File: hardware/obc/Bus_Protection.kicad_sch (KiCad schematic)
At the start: 42 parts, among them Q201 BSS138DWQ-7, Q202 BSS138DWQ-7, Q203 MBT2222ADW1T1, Q204 MBT2222ADW1T1, Q205 BSS138DWQ-7, Q206 BSS138DWQ-7, Q207 MBT2222ADW1T1, Q208 MBT2222ADW1T1, Q209 MMDT2907

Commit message: obc: adjust part numbers for resistors
Many of selected variants are difficult to source for assembly.
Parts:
- R203, R204, R213, R214: LCSC C4244464 -> C112310; Manufacturer_Name Vishay Intertech -> (none); Manufacturer_Part_Number CRCW0603680RJNEA -> (none)
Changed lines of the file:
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@@
 			)
 		)
-		(property "LCSC" "C4244464"
+		(property "LCSC" "C112310"
 			(at 39.37 66.04 0)
 			(effects
@@
 			)
 		)
-		(property "Manufacturer_Name" " Vishay Intertech"
+		(property "Manufacturer_Name" ""
 			(at 39.37 66.04 0)
 			(effects
@@
 			)
 		)
-		(property "Manufacturer_Part_Number" " CRCW0603680RJNEA"
+		(property "Manufacturer_Part_Number" ""
 			(at 39.37 66.04 0)
 			(effects
@@
 			)
 		)
-		(property "LCSC" "C4244464"
+		(property "LCSC" "C112310"
 			(at 81.28 66.04 0)
 			(effects
@@
 			)
 		)
-		(property "Manufacturer_Name" " Vishay Intertech"
+		(property "Manufacturer_Name" ""
 			(at 81.28 66.04 0)
 			(effects
@@
 			)
 		)
-		(property "Manufacturer_Part_Number" " CRCW0603680RJNEA"
+		(property "Manufacturer_Part_Number" ""
 			(at 81.28 66.04 0)
 			(effects
@@
 			)
 		)
-		(property "LCSC" "C4244464"
+		(property "LCSC" "C112310"
 			(at 39.37 144.78 0)
 			(effects
@@
 			)
 		)
-		(property "Manufacturer_Name" " Vishay Intertech"
+		(property "Manufacturer_Name" ""
 			(at 39.37 144.78 0)
 			(effects
@@
 			)
 		)
-		(property "Manufacturer_Part_Number" " CRCW0603680RJNEA"
+		(property "Manufacturer_Part_Number" ""
 			(at 39.37 144.78 0)
 			(effects
@@
 			)
 		)
-		(property "LCSC" "C4244464"
+		(property "LCSC" "C112310"
 			(at 81.28 144.78 0)
 			(effects
@@
 			)
 		)
-		(property "Manufacturer_Name" " Vishay Intertech"
+		(property "Manufacturer_Name" ""
 			(at 81.28 144.78 0)
 			(effects
@@
 			)
 		)
-		(property "Manufacturer_Part_Number" " CRCW0603680RJNEA"
+		(property "Manufacturer_Part_Number" ""
 			(at 81.28 144.78 0)
 			(effects

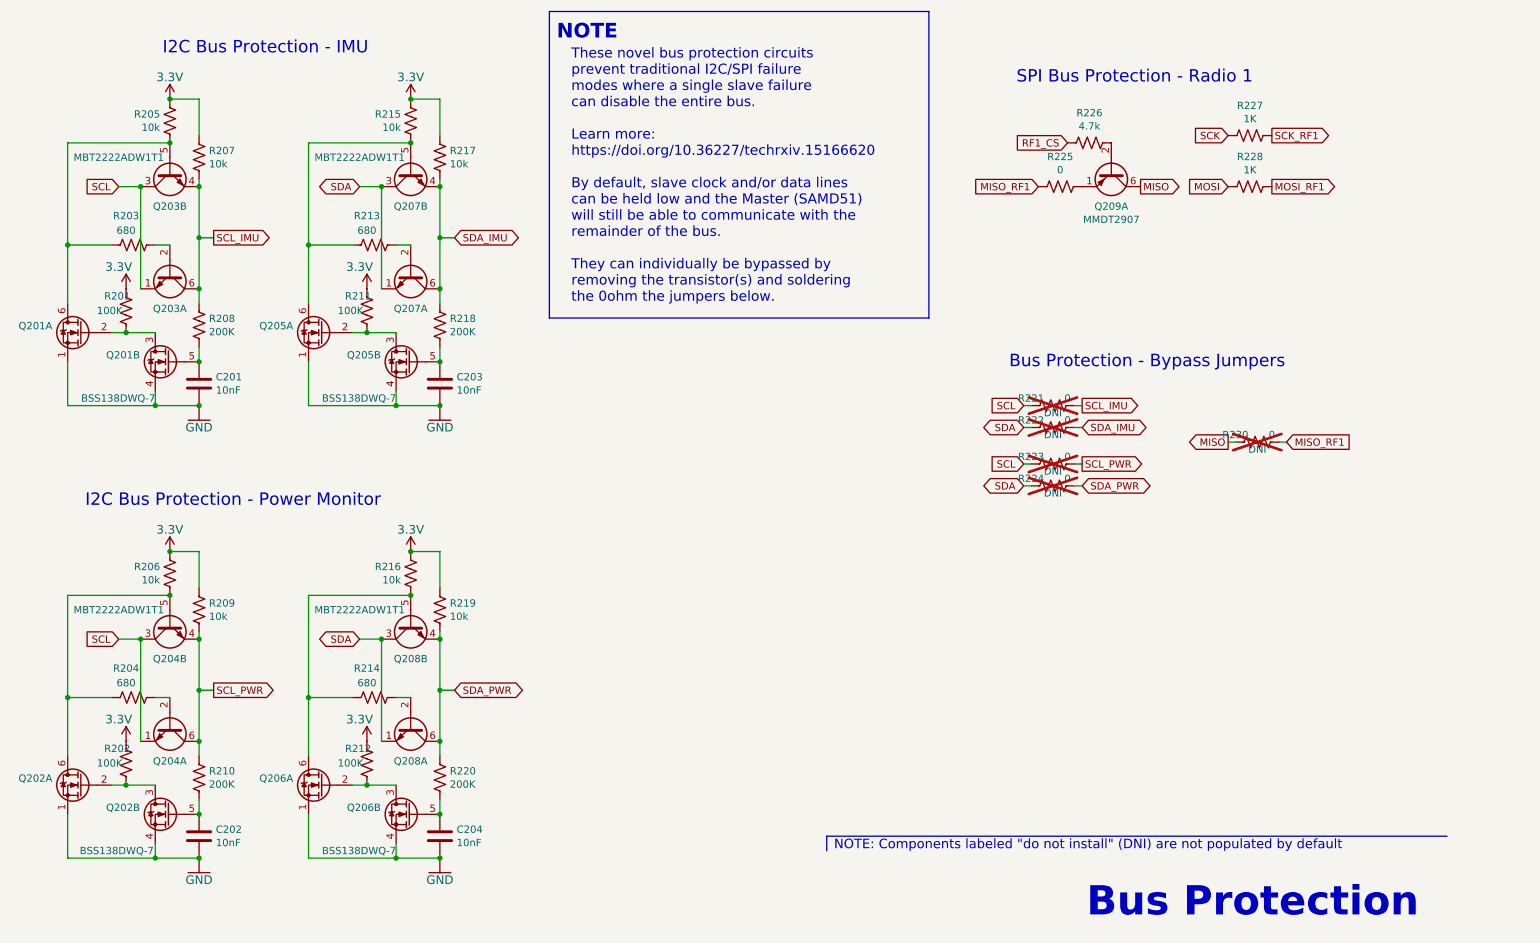
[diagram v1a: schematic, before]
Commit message: obc: substitute transistors based on study of datasheets
We have struggled with availability and made these substitutions.
Same footprint, so layout doesn't change:

ON BSS138DWQ-7-F -> Nexperia BSS138PS,115

ON MMDT2907AQ-7-F -> Nexperia BC857BS,115
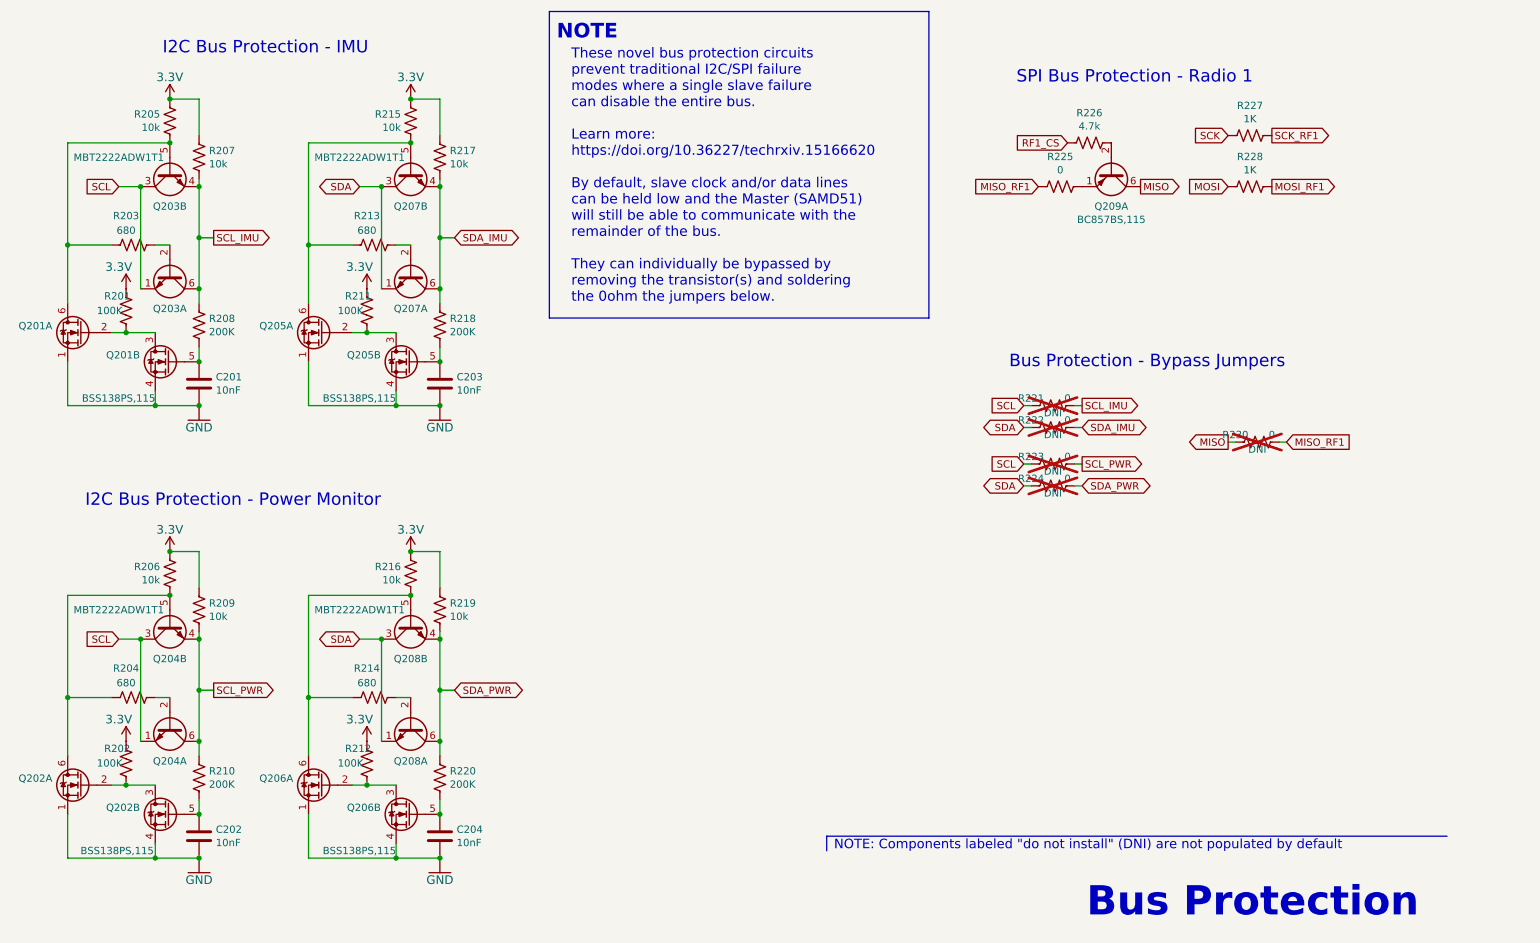
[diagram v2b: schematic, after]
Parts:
- Q201, Q202, Q205, Q206: value BSS138DWQ-7 -> BSS138PS,115; Flight BSS138DWQ-7 -> BSS138PS,115; LCSC C3280240 -> C193381; Manufacturer_Name Diodes Incorporated -> (none); Manufacturer_Part_Number BSS138DWQ-7 -> BSS138PS,115; Proto BSS138DWQ-7 -> BSS138PS,115
- Q209: value MMDT2907 -> BC857BS,115; Flight MMDT2907AQ-7-F -> BC857BS,115; LCSC C526684 -> C8654; Manufacturer_Name Diodes Incorporated -> (none); Manufacturer_Part_Number MMDT2907AQ-7-F -> BC857BS,115; Proto MMDT2907A -> BC857BS,115
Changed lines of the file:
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@@
 			)
 		)
-		(property "Value" "BSS138DWQ-7"
+		(property "Value" "BSS138PS,115"
 			(at 43.18 92.71 0)
 			(effects
@@
 			)
 		)
-		(property "Flight" "BSS138DWQ-7"
+		(property "Flight" "BSS138PS,115"
 			(at 29.21 81.28 0)
 			(effects
@@
 			)
 		)
-		(property "Manufacturer_Name" "Diodes Incorporated"
+		(property "Manufacturer_Name" ""
 			(at 25.4 87.63 0)
 			(effects
@@
 			)
 		)
-		(property "Manufacturer_Part_Number" " BSS138DWQ-7"
+		(property "Manufacturer_Part_Number" "BSS138PS,115"
 			(at 25.4 90.17 0)
 			(effects
@@
 			)
 		)
-		(property "Proto" "BSS138DWQ-7"
+		(property "Proto" "BSS138PS,115"
 			(at 29.21 81.28 0)
 			(effects
@@
 			)
 		)
-		(property "LCSC" "C3280240"
+		(property "LCSC" "C193381"
 			(at 29.21 81.28 0)
 			(effects
@@
 			)
 		)
-		(property "Value" "BSS138DWQ-7"
+		(property "Value" "BSS138PS,115"
 			(at 48.26 91.44 0)
 			(effects
@@
 			)
 		)
-		(property "Flight" "BSS138DWQ-7"
+		(property "Flight" "BSS138PS,115"
 			(at 44.45 86.36 0)
 			(effects
@@
 			)
 		)
-		(property "Manufacturer_Name" "Diodes Incorporated"
+		(property "Manufacturer_Name" ""
 			(at 40.64 92.71 0)
 			(effects
@@
 			)
 		)
-		(property "Manufacturer_Part_Number" " BSS138DWQ-7"
+		(property "Manufacturer_Part_Number" "BSS138PS,115"
 			(at 40.64 95.25 0)
 			(effects
@@
 			)
 		)
-		(property "Proto" "BSS138DWQ-7"
+		(property "Proto" "BSS138PS,115"
 			(at 44.45 86.36 0)
 			(effects
@@
 			)
 		)
-		(property "LCSC" "C3280240"
+		(property "LCSC" "C193381"
 			(at 44.45 86.36 0)
 			(effects
@@
 			)
 		)
-		(property "Value" "BSS138DWQ-7"
+		(property "Value" "BSS138PS,115"
 			(at 90.17 91.44 0)
 			(effects
@@
 			)
 		)
-		(property "Flight" "BSS138DWQ-7"
+		(property "Flight" "BSS138PS,115"
 			(at 86.36 86.36 0)
 			(effects
@@
 			)
 		)
-		(property "Manufacturer_Name" "Diodes Incorporated"
+		(property "Manufacturer_Name" ""
 			(at 82.55 92.71 0)
 			(effects
@@
 			)
 		)
-		(property "Manufacturer_Part_Number" " BSS138DWQ-7"
+		(property "Manufacturer_Part_Number" "BSS138PS,115"
 			(at 82.55 95.25 0)
 			(effects
@@
 			)
 		)
-		(property "Proto" "BSS138DWQ-7"
+		(property "Proto" "BSS138PS,115"
 			(at 86.36 86.36 0)
 			(effects
@@
 			)
 		)
-		(property "LCSC" "C3280240"
+		(property "LCSC" "C193381"
 			(at 86.36 86.36 0)
 			(effects
@@
 			)
 		)
-		(property "Value" "BSS138DWQ-7"
+		(property "Value" "BSS138PS,115"
 			(at 85.09 92.71 0)
 			(effects
@@
 			)
 		)
-		(property "Flight" "BSS138DWQ-7"
+		(property "Flight" "BSS138PS,115"
 			(at 71.12 81.28 0)
 			(effects
@@
 			)
 		)
-		(property "Manufacturer_Name" "Diodes Incorporated"
+		(property "Manufacturer_Name" ""
 			(at 67.31 87.63 0)
 			(effects
@@
 			)
 		)
-		(property "Manufacturer_Part_Number" " BSS138DWQ-7"
+		(property "Manufacturer_Part_Number" "BSS138PS,115"
 			(at 67.31 90.17 0)
 			(effects
@@
 			)
 		)
-		(property "Proto" "BSS138DWQ-7"
+		(property "Proto" "BSS138PS,115"
 			(at 71.12 81.28 0)
 			(effects
@@
 			)
 		)
-		(property "LCSC" "C3280240"
+		(property "LCSC" "C193381"
 			(at 71.12 81.28 0)
 			(effects
@@
 			)
 		)
-		(property "Value" "BSS138DWQ-7"
+		(property "Value" "BSS138PS,115"
 			(at 48.26 170.18 0)
 			(effects
@@
 			)
 		)
-		(property "Flight" "BSS138DWQ-7"
+		(property "Flight" "BSS138PS,115"
 			(at 44.45 165.1 0)
 			(effects
@@
 			)
 		)
-		(property "Manufacturer_Name" "Diodes Incorporated"
+		(property "Manufacturer_Name" ""
 			(at 40.64 171.45 0)
 			(effects
@@
 			)
 		)
-		(property "Manufacturer_Part_Number" " BSS138DWQ-7"
+		(property "Manufacturer_Part_Number" "BSS138PS,115"
 			(at 40.64 173.99 0)
 			(effects
@@
 			)
 		)
-		(property "Proto" "BSS138DWQ-7"
+		(property "Proto" "BSS138PS,115"
 			(at 44.45 165.1 0)
 			(effects
@@
 			)
 		)
-		(property "LCSC" "C3280240"
+		(property "LCSC" "C193381"
 			(at 44.45 165.1 0)
 			(effects
@@
 			)
 		)
-		(property "Value" "BSS138DWQ-7"
+		(property "Value" "BSS138PS,115"
 			(at 42.926 171.45 0)
 			(effects
@@
 			)
 		)
-		(property "Flight" "BSS138DWQ-7"
+		(property "Flight" "BSS138PS,115"
 			(at 29.21 160.02 0)
 			(effects
@@
 			)
 		)
-		(property "Manufacturer_Name" "Diodes Incorporated"
+		(property "Manufacturer_Name" ""
 			(at 25.4 166.37 0)
 			(effects
@@
 			)
 		)
-		(property "Manufacturer_Part_Number" " BSS138DWQ-7"
+		(property "Manufacturer_Part_Number" "BSS138PS,115"
 			(at 25.4 168.91 0)
 			(effects
@@
 			)
 		)
-		(property "Proto" "BSS138DWQ-7"
+		(property "Proto" "BSS138PS,115"
 			(at 29.21 160.02 0)
 			(effects
@@
 			)
 		)
-		(property "LCSC" "C3280240"
+		(property "LCSC" "C193381"
 			(at 29.21 160.02 0)
 			(effects
@@
 			)
 		)
-		(property "Value" "BSS138DWQ-7"
+		(property "Value" "BSS138PS,115"
 			(at 90.17 170.18 0)
 			(effects
@@
 			)
 		)
-		(property "Flight" "BSS138DWQ-7"
+		(property "Flight" "BSS138PS,115"
 			(at 86.36 165.1 0)
 			(effects
@@
 			)
 		)
-		(property "Manufacturer_Name" "Diodes Incorporated"
+		(property "Manufacturer_Name" ""
 			(at 82.55 171.45 0)
 			(effects
@@
 			)
 		)
-		(property "Manufacturer_Part_Number" " BSS138DWQ-7"
+		(property "Manufacturer_Part_Number" "BSS138PS,115"
 			(at 82.55 173.99 0)
 			(effects
@@
 			)
 		)
-		(property "Proto" "BSS138DWQ-7"
+		(property "Proto" "BSS138PS,115"
 			(at 86.36 165.1 0)
 			(effects
@@
 			)
 		)
-		(property "LCSC" "C3280240"
+		(property "LCSC" "C193381"
 			(at 86.36 165.1 0)
 			(effects
@@
 			)
 		)
-		(property "Value" "BSS138DWQ-7"
+		(property "Value" "BSS138PS,115"
 			(at 85.09 171.45 0)
 			(effects
@@
 			)
 		)
-		(property "Flight" "BSS138DWQ-7"
+		(property "Flight" "BSS138PS,115"
 			(at 71.12 160.02 0)
 			(effects
@@
 			)
 		)
-		(property "Manufacturer_Name" "Diodes Incorporated"
+		(property "Manufacturer_Name" ""
 			(at 67.31 166.37 0)
 			(effects
@@
 			)
 		)
-		(property "Manufacturer_Part_Number" " BSS138DWQ-7"
+		(property "Manufacturer_Part_Number" "BSS138PS,115"
 			(at 67.31 168.91 0)
 			(effects
@@
 			)
 		)
-		(property "Proto" "BSS138DWQ-7"
+		(property "Proto" "BSS138PS,115"
 			(at 71.12 160.02 0)
 			(effects
@@
 			)
 		)
-		(property "LCSC" "C3280240"
+		(property "LCSC" "C193381"
 			(at 71.12 160.02 0)
 			(effects
@@
 			)
 		)
-		(property "Value" "MMDT2907"
+		(property "Value" "BC857BS,115"
 			(at 209.55 61.6204 90)
 			(effects
@@
 			)
 		)
-		(property "Flight" "MMDT2907AQ-7-F"
+		(property "Flight" "BC857BS,115"
 			(at 209.55 53.34 0)
 			(effects
@@
 			)
 		)
-		(property "Manufacturer_Name" "Diodes Incorporated"
+		(property "Manufacturer_Name" ""
 			(at 209.55 53.34 0)
 			(effects
@@
 			)
 		)
-		(property "Manufacturer_Part_Number" "MMDT2907AQ-7-F"
+		(property "Manufacturer_Part_Number" "BC857BS,115"
 			(at 212.09 59.309 0)
 			(effects
@@
 			)
 		)
-		(property "Proto" "MMDT2907A"
+		(property "Proto" "BC857BS,115"
 			(at 209.55 53.34 0)
 			(effects
@@
 			)
 		)
-		(property "LCSC" "C526684"
+		(property "LCSC" "C8654"
 			(at 209.55 53.34 0)
 			(effects

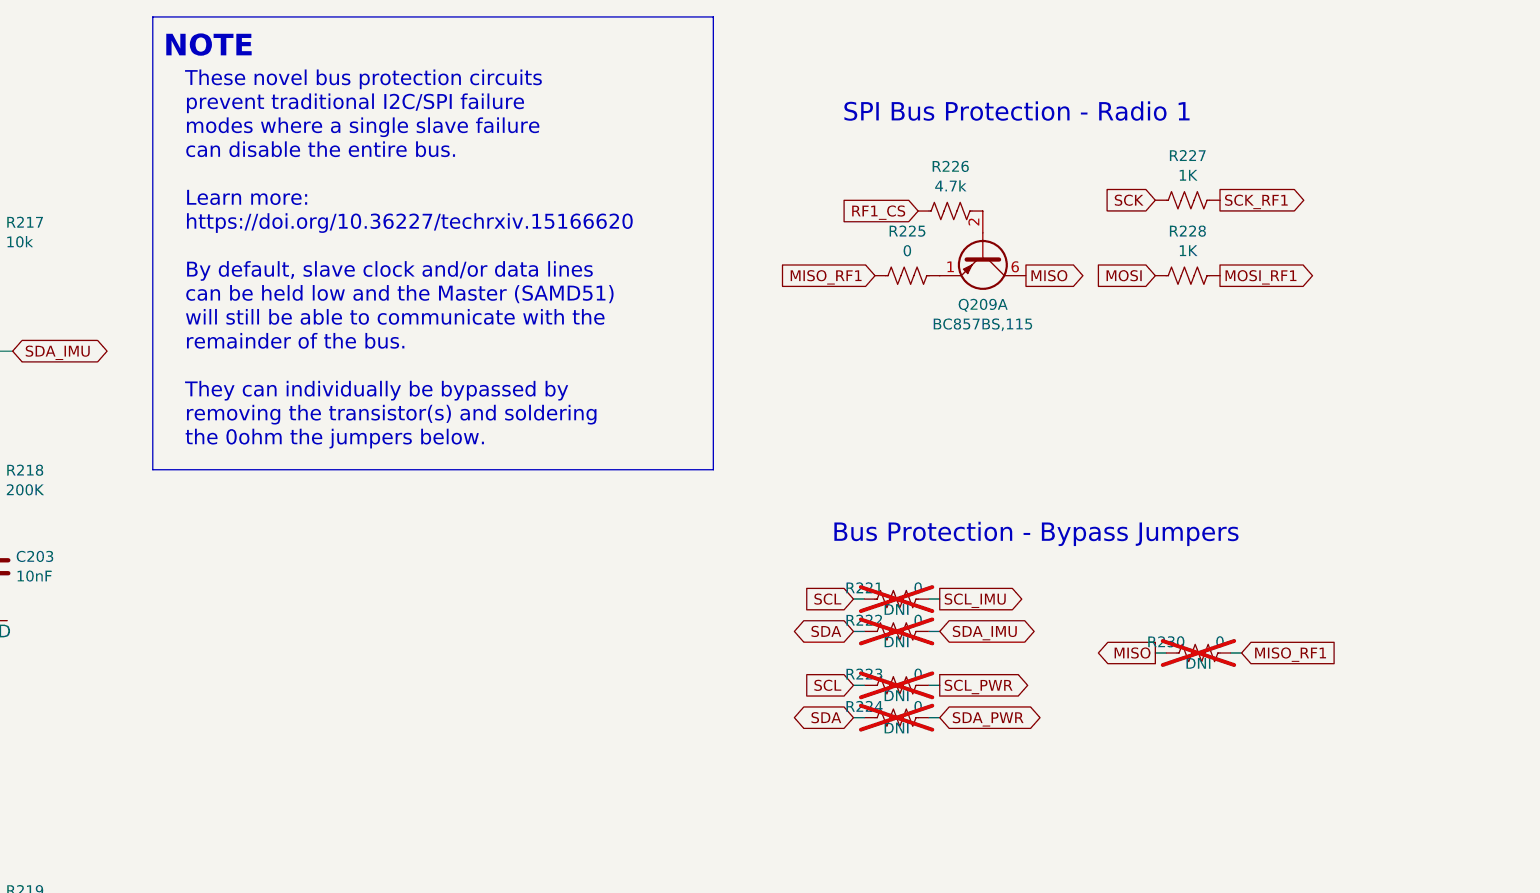
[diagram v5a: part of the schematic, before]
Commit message: OBC: Continuing work towards the next revision
- Changed 3.3V names on Avionics page
- Removed buss protection-bypass jumpers
- Edited SPI buss protection
- Removed U302
- Removed JP401
- Other label/clean up modifications
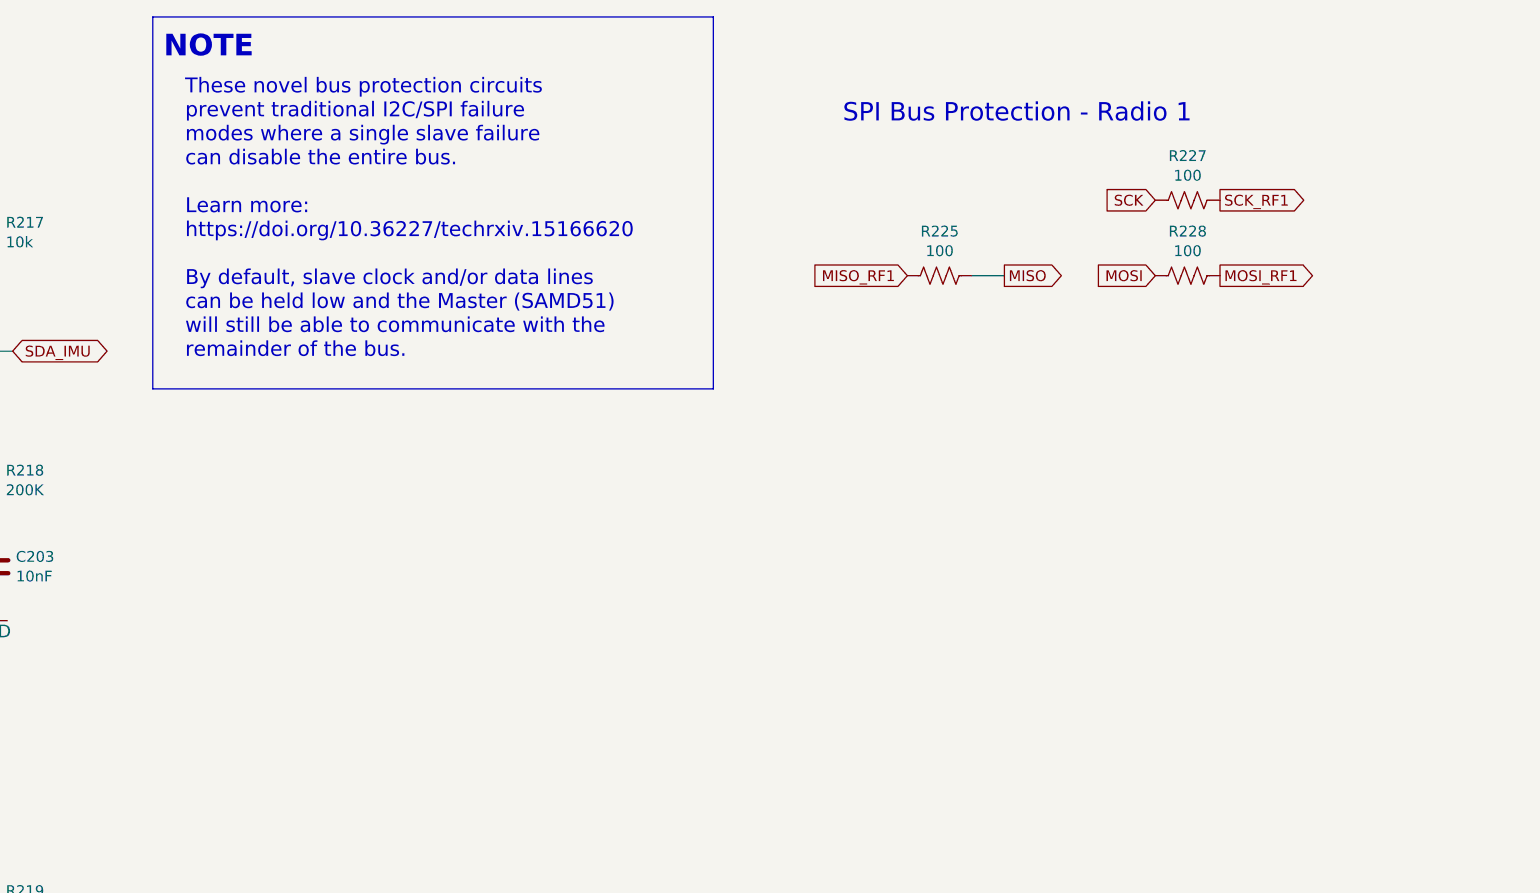
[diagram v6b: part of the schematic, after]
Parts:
- removed Q209: BC857BS,115, Package_TO_SOT_SMD:SOT-363_SC-70-6, symbol mainboard:MMDT2907
- removed R221, R222, R223, R224, R230: 0, Resistor_SMD:R_0603_1608Metric, symbol Device:R_US
- removed R226: 4.7k, Resistor_SMD:R_0603_1608Metric, symbol Device:R_US
- R225: value 0 -> 100; LCSC C2654002 -> (none); Manufacturer_Name Vishay Intertech -> (none); Manufacturer_Part_Number MCT06030Z0000ZP500 -> (none)
- R227, R228: value 1K -> 100; LCSC C844746 -> (none); Manufacturer_Name Vishay Intertech -> (none); Manufacturer_Part_Number CRCW06031K00FKEAC -> (none)
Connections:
- net MISO: now also R225.1
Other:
- note added: "These novel bus protection circuits prevent traditional I2C/SPI failure modes where a single slave failure can disable the entire bus. Learn more: https://doi.org/10.36227/techrxiv.15166620 By default, slave clock and/or data lines can be held low and the Master (SAMD51) will still be able to communicate with the remainder of the bus."
- note removed: "Bus Protection - Bypass Jumpers"
- note removed: "These novel bus protection circuits prevent traditional I2C/SPI failure modes where a single slave failure can disable the entire bus. Learn more: https://doi.org/10.36227/techrxiv.15166620 By default, slave clock and/or data lines can be held low and the Master (SAMD51) will still be able to communicate with the remainder of the bus. They can individually be bypassed by removing the transistor(s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"
- moved on the sheet: R225
